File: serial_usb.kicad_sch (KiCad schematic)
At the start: 24 parts, among them J2 3V3 Serial, J3 USB_C_USB2.0_16P, U17 ST16C550, U18 CP2102N, Y2 7.3728MHz

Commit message: merge in rev4
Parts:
- removed R16: 47k, Resistor_SMD:R_0402_1005Metric, symbol Device:R_Small
- added U23: 74AHC1GU04, Package_TO_SOT_SMD:SOT-23-5, symbol 74xGxx:74AHC1GU04
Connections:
- net +3V3: now also U23.5 (VCC)
- net GND: now also C31.2, U23.3 (GND)
- net at U17.35 (RESET): now also U23.4; no longer C31.2
- new net ~{RESET}: U23.2

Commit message: fix address decoding
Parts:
- C31, C36, C38: LCSC (none) -> C466613
- C34, C35: LCSC (none) -> C2183219
- C37: LCSC (none) -> C2226854
- D7, D8: LCSC (none) -> C5246833
- D9: LCSC (none) -> C5337181
- J3: LCSC (none) -> C2909599
- R17, R18: LCSC (none) -> C375970
- R19, R23: LCSC (none) -> C478865
- R20, R25: LCSC (none) -> C384321
- R21: LCSC (none) -> C328306
- R22: LCSC (none) -> C3015870
- R24: LCSC (none) -> C2929993
- U17: LCSC (none) -> C42754
- U18: LCSC (none) -> C969913
- U23: LCSC (none) -> C352954
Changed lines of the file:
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@@
 	(title_block
 		(title "NS32016 Toy PCB")
-		(date "2024-08-01")
+		(date "2024-08-10")
 		(rev "Rev 4")
 		(comment 1 "bson@rockgarden.net")
@@
 			)
 		)
+		(property "LCSC" "C478865"
+			(at 198.12 166.37 0)
+			(effects
+				(font
+					(size 1.27 1.27)
+				)
+				(hide yes)
+			)
+		)
 		(pin "1"
 		)
@@
 			)
 		)
+		(property "LCSC" "C466613"
+			(at 165.1 40.64 0)
+			(effects
+				(font
+					(size 1.27 1.27)
+				)
+				(hide yes)
+			)
+		)
 		(pin "1"
 		)
@@
 			)
 		)
+		(property "LCSC" "C478865"
+			(at 190.5 166.37 0)
+			(effects
+				(font
+					(size 1.27 1.27)
+				)
+				(hide yes)
+			)
+		)
 		(pin "1"
 		)
@@
 			)
 		)
+		(property "LCSC" "C2183219"
+			(at 171.45 200.66 0)
+			(effects
+				(font
+					(size 1.27 1.27)
+				)
+				(hide yes)
+			)
+		)
 		(pin "2"
 		)
@@
 			)
 		)
+		(property "LCSC" "C5246833"
+			(at 198.12 173.99 0)
+			(effects
+				(font
+					(size 1.27 1.27)
+				)
+				(hide yes)
+			)
+		)
 		(pin "1"
 		)
@@
 			)
 		)
+		(property "LCSC" "C969913"
+			(at 232.41 167.64 0)
+			(effects
+				(font
+					(size 1.27 1.27)
+				)
+				(hide yes)
+			)
+		)
 		(pin "20"
 		)
@@
 			)
 		)
+		(property "LCSC" "C42754"
+			(at 163.83 151.13 0)
+			(effects
+				(font
+					(size 1.27 1.27)
+				)
+				(hide yes)
+			)
+		)
 		(pin "1"
 		)
@@
 			)
 		)
+		(property "LCSC" "C466613"
+			(at 130.81 60.96 0)
+			(effects
+				(font
+					(size 1.27 1.27)
+				)
+				(hide yes)
+			)
+		)
 		(pin "1"
 		)
@@
 			)
 		)
+		(property "LCSC" "C352954"
+			(at 147.32 76.2 0)
+			(effects
+				(font
+					(size 1.27 1.27)
+				)
+				(hide yes)
+			)
+		)
 		(pin "3"
 		)
@@
 			)
 		)
+		(property "LCSC" "C328306"
+			(at 165.1 185.42 0)
+			(effects
+				(font
+					(size 1.27 1.27)
+				)
+				(hide yes)
+			)
+		)
 		(pin "2"
 		)
@@
 			)
 		)
+		(property "LCSC" "C2226854"
+			(at 219.71 128.27 0)
+			(effects
+				(font
+					(size 1.27 1.27)
+				)
+				(hide yes)
+			)
+		)
 		(pin "1"
 		)
@@
 			)
 		)
+		(property "LCSC" "C42754"
+			(at 172.72 60.96 0)
+			(effects
+				(font
+					(size 1.27 1.27)
+				)
+				(hide yes)
+			)
+		)
 		(pin "35"
 		)
@@
 			)
 		)
+		(property "LCSC" "C2183219"
+			(at 158.75 200.66 0)
+			(effects
+				(font
+					(size 1.27 1.27)
+				)
+				(hide yes)
+			)
+		)
 		(pin "2"
 		)
@@
 			)
 		)
+		(property "LCSC" "C5337181"
+			(at 265.43 182.88 0)
+			(effects
+				(font
+					(size 1.27 1.27)
+				)
+				(hide yes)
+			)
+		)
 		(pin "2"
 		)
@@
 			)
 		)
+		(property "LCSC" "C5246833"
+			(at 190.5 173.99 0)
+			(effects
+				(font
+					(size 1.27 1.27)
+				)
+				(hide yes)
+			)
+		)
 		(pin "1"
 		)
@@
 			)
 		)
+		(property "LCSC" "C375970"
+			(at 201.93 137.16 0)
+			(effects
+				(font
+					(size 1.27 1.27)
+				)
+				(hide yes)
+			)
+		)
 		(pin "1"
 		)
@@
 			)
 		)
+		(property "LCSC" "C466613"
+			(at 224.79 128.27 0)
+			(effects
+				(font
+					(size 1.27 1.27)
+				)
+				(hide yes)
+			)
+		)
 		(pin "1"
 		)
@@
 			)
 		)
+		(property "LCSC" "C3015870"
+			(at 264.16 156.21 0)
+			(effects
+				(font
+					(size 1.27 1.27)
+				)
+				(hide yes)
+			)
+		)
 		(pin "2"
 		)
@@
 			)
 		)
+		(property "LCSC" "C2929993"
+			(at 259.08 151.13 0)
+			(effects
+				(font
+					(size 1.27 1.27)
+				)
+				(hide yes)
+			)
+		)
 		(pin "1"
 		)
@@
 			)
 		)
+		(property "LCSC" "C2909599"
+			(at 308.61 166.37 0)
+			(effects
+				(font
+					(size 1.27 1.27)
+				)
+				(hide yes)
+			)
+		)
 		(pin "A1"
 		)
@@
 			)
 		)
+		(property "LCSC" "C375970"
+			(at 246.38 138.43 0)
+			(effects
+				(font
+					(size 1.27 1.27)
+				)
+				(hide yes)
+			)
+		)
 		(pin "2"
 		)
@@
 			)
 		)
+		(property "LCSC" "C384321"
+			(at 289.56 180.34 0)
+			(effects
+				(font
+					(size 1.27 1.27)
+				)
+				(hide yes)
+			)
+		)
 		(pin "2"
 		)
@@
 			(at 280.67 180.34 0)
 			(effects
+				(font
+					(size 1.27 1.27)
+				)
+				(hide yes)
+			)
+		)
+		(property "LCSC" "C384321"
+			(at 280.67 180.34 0)
+			(effects

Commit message: add rev4 gerbers, bom files
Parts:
- J2: value 3V3 Serial -> 3V3 Serial DNP
- Y2: value 7.3728MHz -> 7.3728MHz DNP
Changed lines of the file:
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@@
 			)
 		)
-		(property "Value" "7.3728MHz"
+		(property "Value" "7.3728MHz DNP"
 			(at 174.244 194.564 0)
 			(effects
@@
 			)
 		)
-		(property "Value" "3V3 Serial"
+		(property "Value" "3V3 Serial DNP"
 			(at 288.29 101.5999 0)
 			(effects

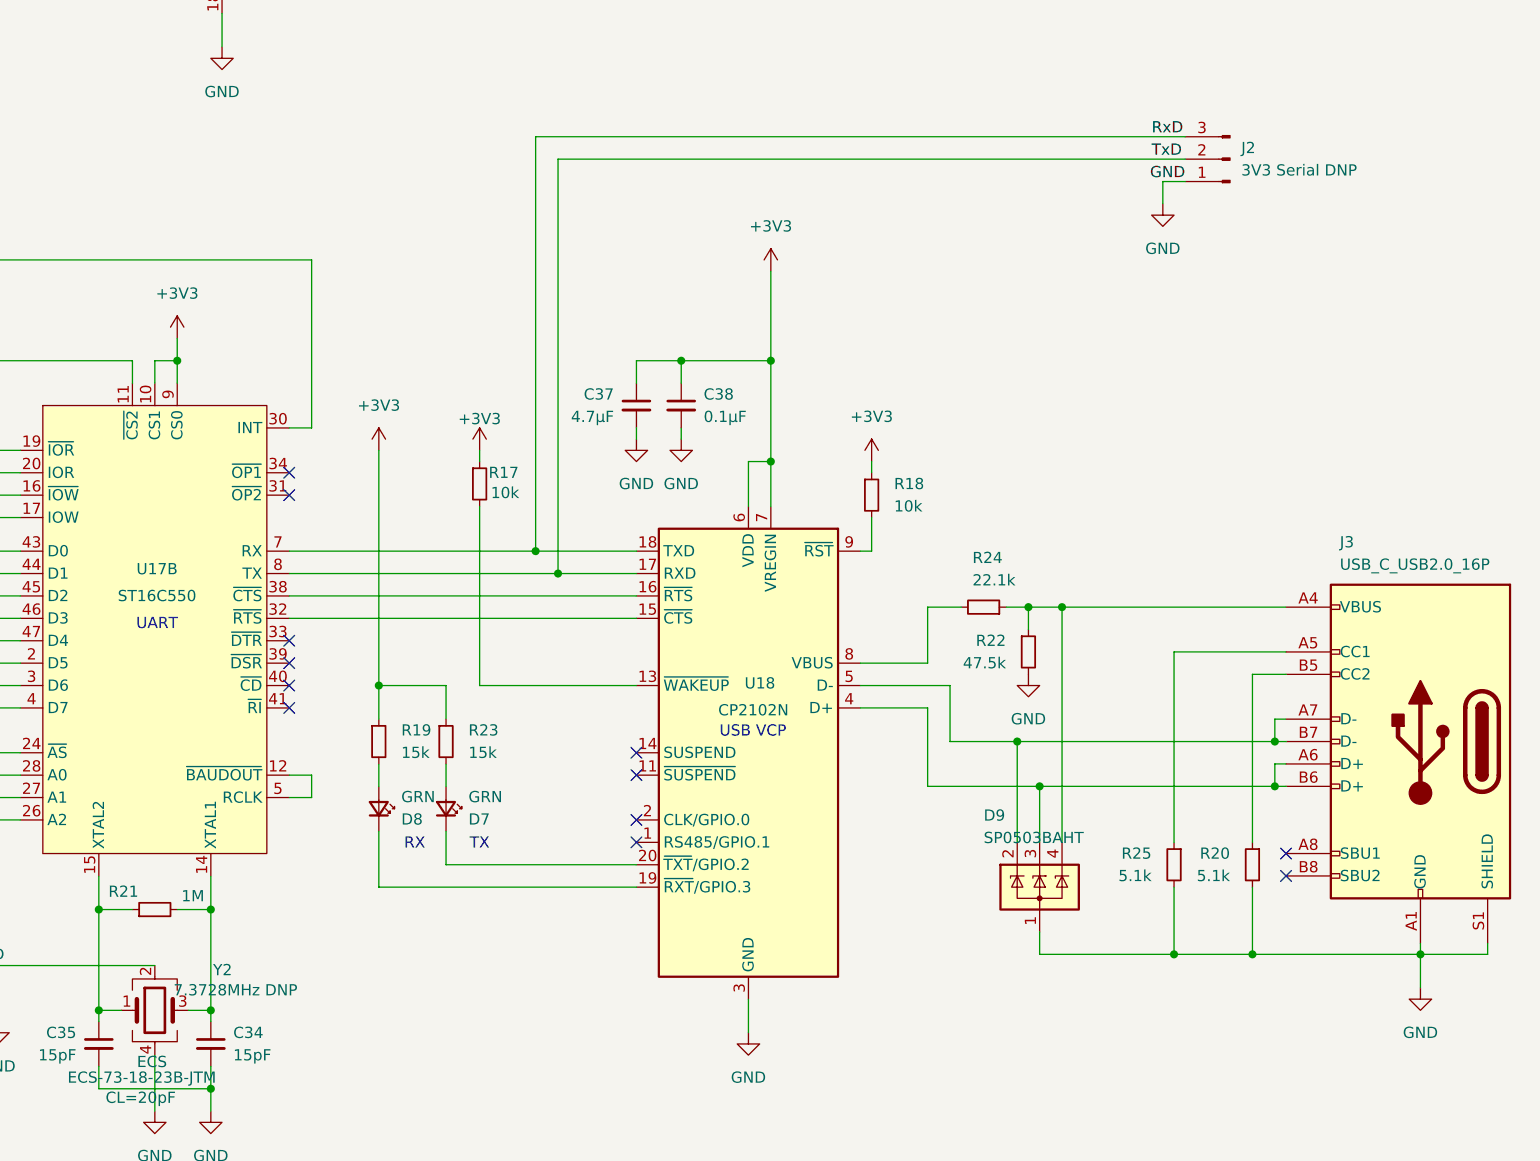
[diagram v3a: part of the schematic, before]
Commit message: various changes, add LCSC part #s
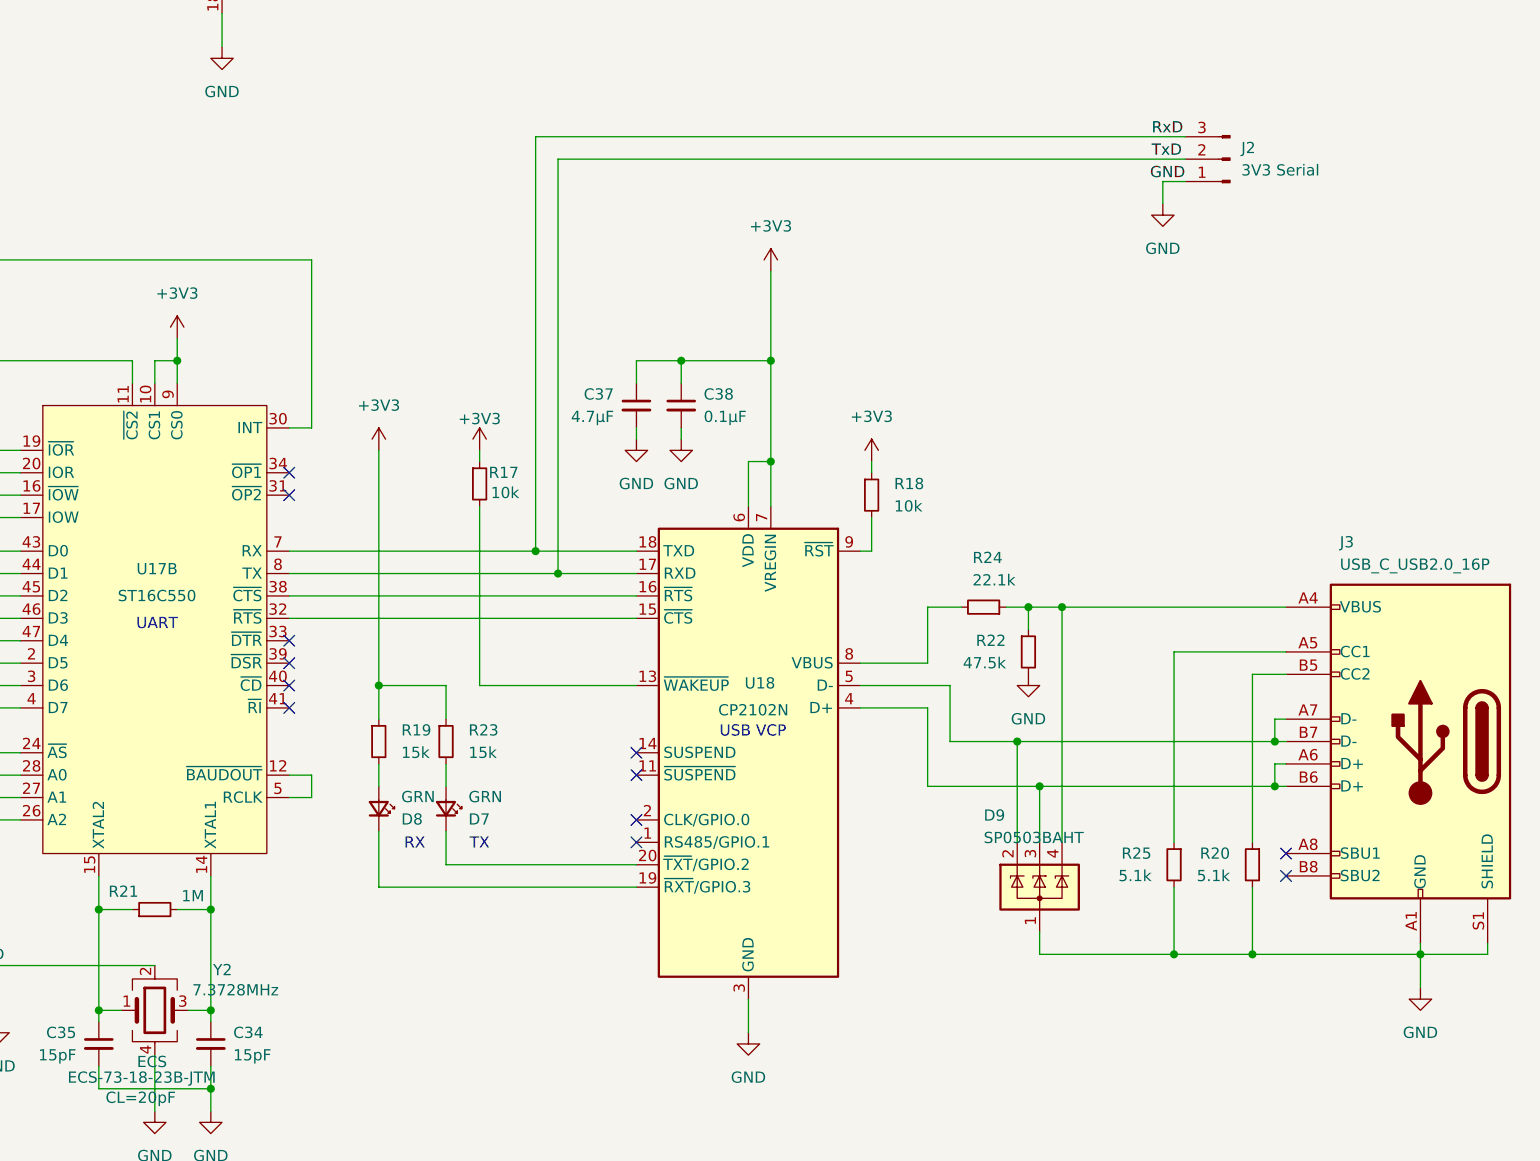
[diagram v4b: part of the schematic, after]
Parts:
- C31, C36, C38: LCSC C466613 -> C3012376
- C34, C35: LCSC C2183219 -> C1852854
- C37: LCSC C2226854 -> C84718
- J2: value 3V3 Serial DNP -> 3V3 Serial
- R19, R23: LCSC C478865 -> C850820
- R21: LCSC C328306 -> C4334825
- U17: LCSC C42754 -> C2653190
- U23: LCSC C352954 -> C22384791
- Y2: value 7.3728MHz DNP -> 7.3728MHz
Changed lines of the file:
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@@
 			)
 		)
-		(property "LCSC" "C478865"
+		(property "LCSC" "C850820"
 			(at 198.12 166.37 0)
 			(effects
@@
 			)
 		)
-		(property "LCSC" "C466613"
+		(property "LCSC" "C3012376"
 			(at 165.1 40.64 0)
 			(effects
@@
 			)
 		)
-		(property "LCSC" "C478865"
+		(property "LCSC" "C850820"
 			(at 190.5 166.37 0)
 			(effects
@@
 			)
 		)
-		(property "LCSC" "C2183219"
+		(property "LCSC" "C1852854"
 			(at 171.45 200.66 0)
 			(effects
@@
 			)
 		)
-		(property "LCSC" "C42754"
+		(property "LCSC" "C2653190"
 			(at 163.83 151.13 0)
 			(effects
@@
 			)
 		)
-		(property "LCSC" "C466613"
+		(property "LCSC" "C3012376"
 			(at 130.81 60.96 0)
 			(effects
@@
 			)
 		)
-		(property "LCSC" "C352954"
+		(property "LCSC" "C22384791"
 			(at 147.32 76.2 0)
 			(effects
@@
 			)
 		)
-		(property "LCSC" "C328306"
+		(property "LCSC" "C4334825"
 			(at 165.1 185.42 0)
 			(effects
@@
 			)
 		)
-		(property "LCSC" "C2226854"
+		(property "LCSC" "C84718"
 			(at 219.71 128.27 0)
 			(effects
@@
 			)
 		)
-		(property "LCSC" "C42754"
+		(property "LCSC" "C2653190"
 			(at 172.72 60.96 0)
 			(effects
@@
 			)
 		)
-		(property "LCSC" "C2183219"
+		(property "LCSC" "C1852854"
 			(at 158.75 200.66 0)
 			(effects
@@
 			)
 		)
-		(property "Value" "7.3728MHz DNP"
+		(property "Value" "7.3728MHz"
 			(at 174.244 194.564 0)
 			(effects
@@
 			)
 		)
-		(property "LCSC" "C466613"
+		(property "LCSC" "C3012376"
 			(at 224.79 128.27 0)
 			(effects
@@
 			)
 		)
-		(property "Value" "3V3 Serial DNP"
+		(property "Value" "3V3 Serial"
 			(at 288.29 101.5999 0)
 			(effects

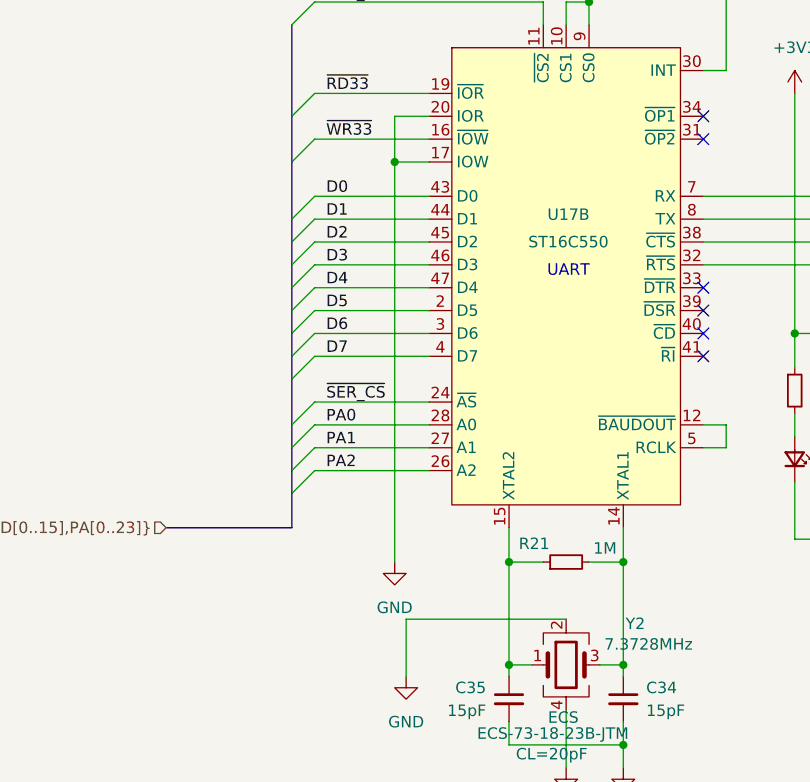
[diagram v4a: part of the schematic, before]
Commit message: AS is active high, and we tie it to GND
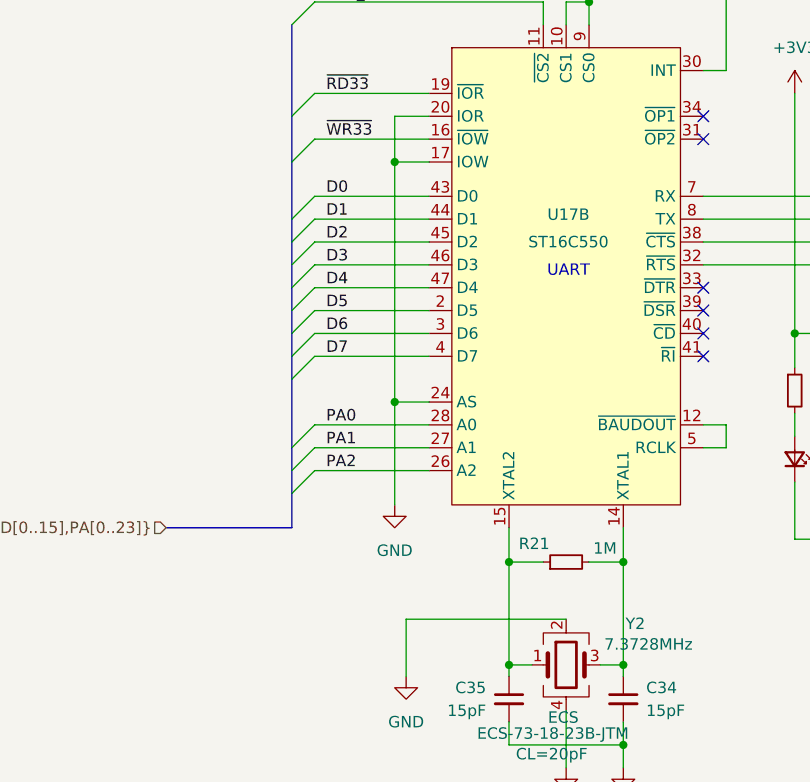
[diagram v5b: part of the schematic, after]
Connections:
- net GND: now also U17.24 (AS)
- net ~{SER_CS}: no longer U17.24 (~{AS})
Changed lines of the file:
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@@
 	)
 	(junction
+		(at 146.05 167.64)
+		(diameter 0)
+		(color 0 0 0 0)
+	)
+	(junction
 		(at 146.05 140.97)
 		(diameter 0)
@@
 	)
 	(bus_entry
-		(at 137.16 167.64)
-		(size -2.54 2.54)
-		(stroke
-			(width 0)
-			(type default)
-		)
-	)
-	(bus_entry
 		(at 134.62 140.97)
 		(size 2.54 -2.54)
@@
 	(wire
 		(pts
-			(xy 137.16 167.64) (xy 149.86 167.64)
-		)
-		(stroke
-			(width 0)
-			(type default)
-		)
-	)
-	(wire
-		(pts
 			(xy 130.81 63.5) (xy 130.81 66.04)
 		)
@@
 	(wire
 		(pts
-			(xy 146.05 185.42) (xy 146.05 140.97)
+			(xy 146.05 179.07) (xy 146.05 167.64)
 		)
 		(stroke
@@
 		)
 	)
-	(bus
-		(pts
-			(xy 134.62 170.18) (xy 134.62 172.72)
-		)
-		(stroke
-			(width 0)
-			(type default)
-		)
-	)
 	(wire
 		(pts
@@
 	(wire
 		(pts
+			(xy 146.05 167.64) (xy 149.86 167.64)
+		)
+		(stroke
+			(width 0)
+			(type default)
+		)
+	)
+	(wire
+		(pts
 			(xy 201.93 134.62) (xy 201.93 133.35)
 		)
@@
 	(wire
 		(pts
+			(xy 146.05 167.64) (xy 146.05 140.97)
+		)
+		(stroke
+			(width 0)
+			(type default)
+		)
+	)
+	(wire
+		(pts
 			(xy 246.38 144.78) (xy 245.11 144.78)
 		)
@@
 	(bus
 		(pts
-			(xy 134.62 165.1) (xy 134.62 170.18)
+			(xy 134.62 165.1) (xy 134.62 172.72)
 		)
 		(stroke
@@
 		)
 	)
-	(label "~{SER_CS}"
-		(at 138.43 167.64 0)
-		(fields_autoplaced yes)
-		(effects
-			(font
-				(size 1.27 1.27)
-			)
-			(justify left bottom)
-		)
-	)
 	(hierarchical_label "{~{SER_CS},~{RD33},~{WR33},D[0..15],PA[0..23]}"
 		(shape input)
@@
 	(symbol
 		(lib_id "power:GND")
-		(at 146.05 185.42 0)
+		(at 146.05 179.07 0)
 		(unit 1)
 		(exclude_from_sim no)
@@
 		(fields_autoplaced yes)
 		(property "Reference" "#PWR053"
-			(at 146.05 191.77 0)
+			(at 146.05 185.42 0)
 			(effects
 				(font
@@
 		)
 		(property "Value" "GND"
-			(at 146.05 190.5 0)
+			(at 146.05 184.15 0)
 			(effects
 				(font
@@
 		)
 		(property "Footprint" ""
-			(at 146.05 185.42 0)
+			(at 146.05 179.07 0)
 			(effects
 				(font
@@
 		)
 		(property "Datasheet" ""
-			(at 146.05 185.42 0)
+			(at 146.05 179.07 0)
 			(effects
 				(font
@@
 		)
 		(property "Description" "Power symbol creates a global label with name \"GND\" , ground"
-			(at 146.05 185.42 0)
+			(at 146.05 179.07 0)
 			(effects
 				(font
@@
 	)
 	(symbol
+		(lib_name "ST16C550_1")
 		(lib_id "ST16C550:ST16C550")
 		(at 163.83 151.13 0)

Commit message: fix a few bugs
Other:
- title: NS32016 Toy PCB -> Toy32k
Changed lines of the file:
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@@
 	(paper "A3")
 	(title_block
-		(title "NS32016 Toy PCB")
-		(date "2024-08-10")
-		(rev "Rev 4")
+		(title "Toy32k")
+		(date "2024-08-16")
+		(rev "Rev 5")
 		(comment 1 "bson@rockgarden.net")
 		(comment 2 "Jan Brittenson")
@@
 	)
 	(junction
+		(at 146.05 167.64)
+		(diameter 0)
+		(color 0 0 0 0)
+	)
+	(junction
 		(at 289.56 190.5)
 		(diameter 0)
@@
 	)
 	(junction
-		(at 146.05 167.64)
-		(diameter 0)
-		(color 0 0 0 0)
-	)
-	(junction
 		(at 146.05 140.97)
 		(diameter 0)
@@
 	(wire
 		(pts
-			(xy 146.05 179.07) (xy 146.05 167.64)
+			(xy 146.05 180.34) (xy 146.05 167.64)
 		)
 		(stroke
@@
 	(wire
 		(pts
-			(xy 146.05 167.64) (xy 149.86 167.64)
-		)
-		(stroke
-			(width 0)
-			(type default)
-		)
-	)
-	(wire
-		(pts
 			(xy 201.93 134.62) (xy 201.93 133.35)
 		)
@@
 	(wire
 		(pts
-			(xy 146.05 167.64) (xy 146.05 140.97)
-		)
-		(stroke
-			(width 0)
-			(type default)
-		)
-	)
-	(wire
-		(pts
 			(xy 246.38 144.78) (xy 245.11 144.78)
 		)
@@
 	(wire
 		(pts
+			(xy 146.05 167.64) (xy 146.05 140.97)
+		)
+		(stroke
+			(width 0)
+			(type default)
+		)
+	)
+	(wire
+		(pts
 			(xy 158.75 185.42) (xy 158.75 196.85)
 		)
@@
 		)
 	)
+	(wire
+		(pts
+			(xy 146.05 167.64) (xy 149.86 167.64)
+		)
+		(stroke
+			(width 0)
+			(type default)
+		)
+	)
 	(bus
 		(pts
@@
 	(symbol
 		(lib_id "power:GND")
-		(at 146.05 179.07 0)
+		(at 146.05 180.34 0)
 		(unit 1)
 		(exclude_from_sim no)
@@
 		(fields_autoplaced yes)
 		(property "Reference" "#PWR053"
-			(at 146.05 185.42 0)
+			(at 146.05 186.69 0)
 			(effects
 				(font
@@
 		)
 		(property "Value" "GND"
-			(at 146.05 184.15 0)
+			(at 146.05 185.42 0)
 			(effects
 				(font
@@
 		)
 		(property "Footprint" ""
-			(at 146.05 179.07 0)
+			(at 146.05 180.34 0)
 			(effects
 				(font
@@
 		)
 		(property "Datasheet" ""
-			(at 146.05 179.07 0)
+			(at 146.05 180.34 0)
 			(effects
 				(font
@@
 		)
 		(property "Description" "Power symbol creates a global label with name \"GND\" , ground"
-			(at 146.05 179.07 0)
+			(at 146.05 180.34 0)
 			(effects
 				(font
@@
 	)
 	(symbol
-		(lib_name "ST16C550_1")
 		(lib_id "ST16C550:ST16C550")
 		(at 163.83 151.13 0)
